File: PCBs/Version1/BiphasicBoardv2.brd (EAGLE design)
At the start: 28.6 x 17.9 mm, 15 parts

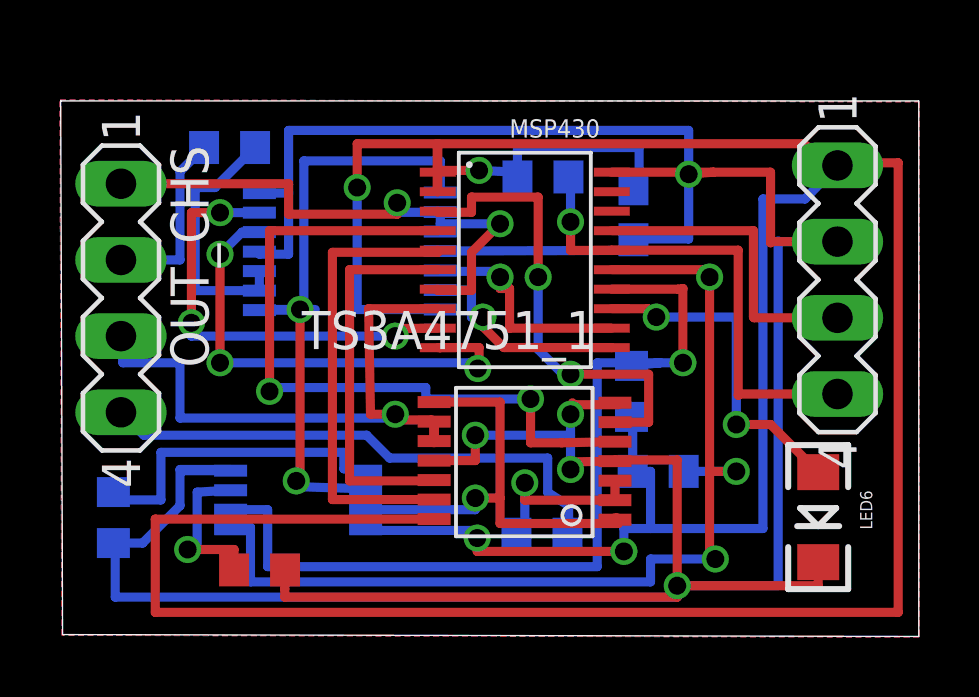
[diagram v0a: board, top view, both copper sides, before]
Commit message: Version 1.1 Changes 1) Added a voltage divider to measure power supply level 2) Removed impedence measurement in one of the biphasic current output channels
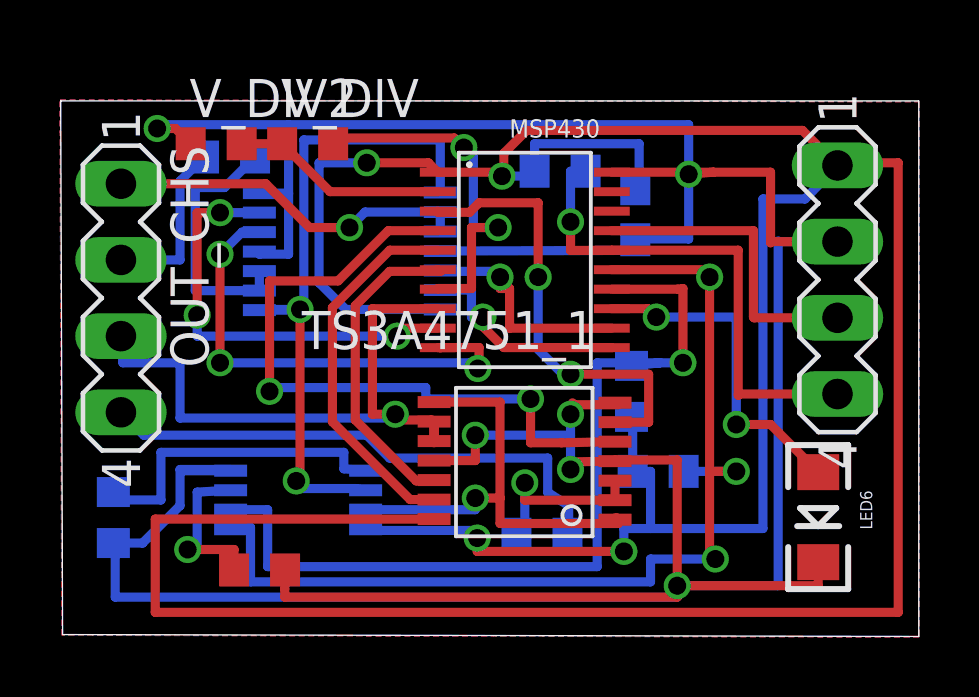
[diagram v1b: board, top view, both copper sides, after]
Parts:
- added V_DIV, V_DIV2: 1M, BiphasicBoard:R0603
- moved R_PULLUP_RST 0.60 mm to (16.6, 15.5)
- moved R_INPUT_FS3 0.32 mm to (5.59, 15.9)
- moved C1_SUPPLY 0.06 mm to (19.1, 14.0)
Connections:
- new net N$6: MSP430.7, V_DIV.2
- new net N$7: MSP430.2, V_DIV.1, V_DIV2.2
- net GND: now also V_DIV2.1
- net LOAD2_0: no longer MSP430.7
- net VDD: no longer MSP430.2
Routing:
- net N$6: track 0.00 -> 12.3 mm, vias 0 -> 2
- net N$7: track 0.00 -> 7.20 mm
- net LOAD2_0: track 18.8 -> 12.1 mm, vias 2 -> 1
- net GND: track 125.7 -> 131.8 mm, vias 5 -> 6
- net IN1_1: track 15.2 -> 12.6 mm
- net VDD: track 124.9 -> 122.5 mm
- net IN4_1: track 12.8 -> 10.7 mm
- net CURRENT0: track 22.2 -> 23.2 mm
- net IN2_1: track 24.4 -> 23.5 mm
- net IN3_1: track 15.7 -> 15.1 mm

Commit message: 1) Corrected resistor name&values; 2) Added resistor for LED.
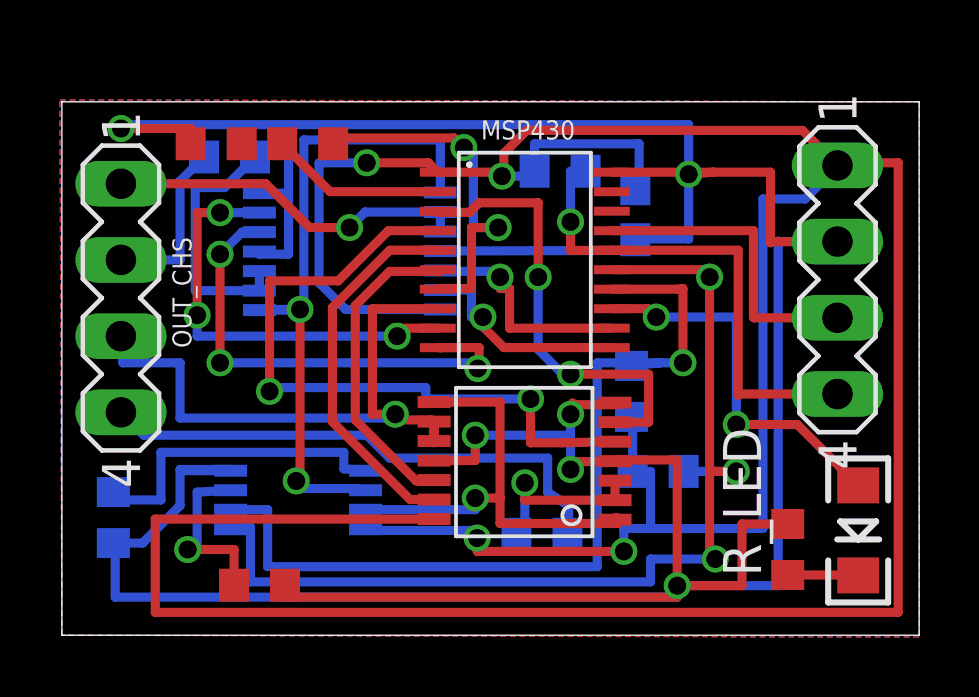
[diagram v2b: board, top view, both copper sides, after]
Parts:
- added R_LED: R_LED, BiphasicBoard:R0603
- R_INPUT_FS1: value 47k -> 43k
- R_LOAD_EX, R_LOAD_EX1: value 47k -> 10k
- R_PULLUP_RST: value (none) -> 43k
- moved LED6 1.41 mm to (26.5, 3.49)
- moved R_INPUT_FS1 0.51 mm to (6.59, 1.67)
- renumbered R_INPUT_FS2 to R_LOAD_EX1, R_INPUT_FS3 to R_LOAD_EX
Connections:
- new net N$9: LED6.C, R_LED.1
- net GND: now also R_LED.2; no longer LED6.C
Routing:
- net GND: track 131.8 -> 134.3 mm
- net N$9: track 0.00 -> 2.36 mm
- net N$5: track 11.2 -> 12.8 mm
- net N$7: track 7.20 -> 5.85 mm
- net VIA1: track 5.58 -> 6.08 mm
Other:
- board size 28.6 x 17.9 mm -> 28.6 x 17.8 mm
- board text added: "GND"
- board text added: "VCC"
